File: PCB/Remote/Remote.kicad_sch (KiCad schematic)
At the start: 51 parts, among them J1 LCD, J2 DC, J3 TEMP, J4 LCD, J5 Reset, J6 USB-C-Socket-H, J7 TC2030-USB-NL-DS, T1 T3902_MEMS_Mic, U1 ESP32-S3-MINI-1, U2 SCD41, U3 MD8942, U4 TMP1075DSG, U5 GZP6816D, U7 SHT40, U8 VEML6040

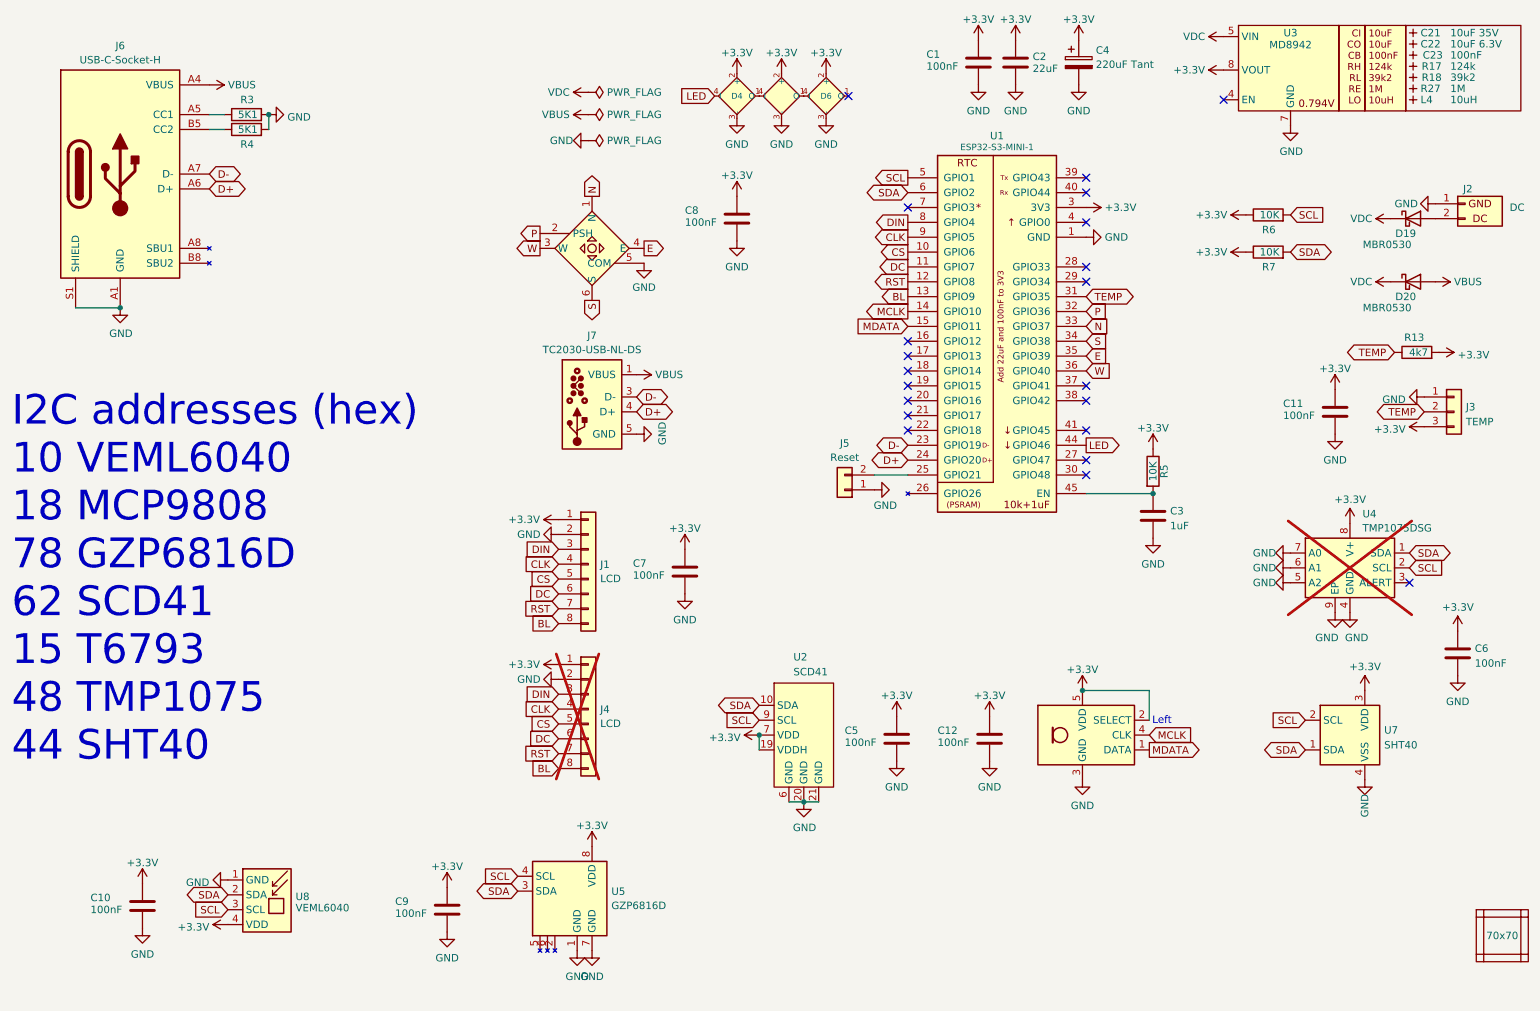
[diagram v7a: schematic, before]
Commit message: Reworked for connecting switch/SCD41
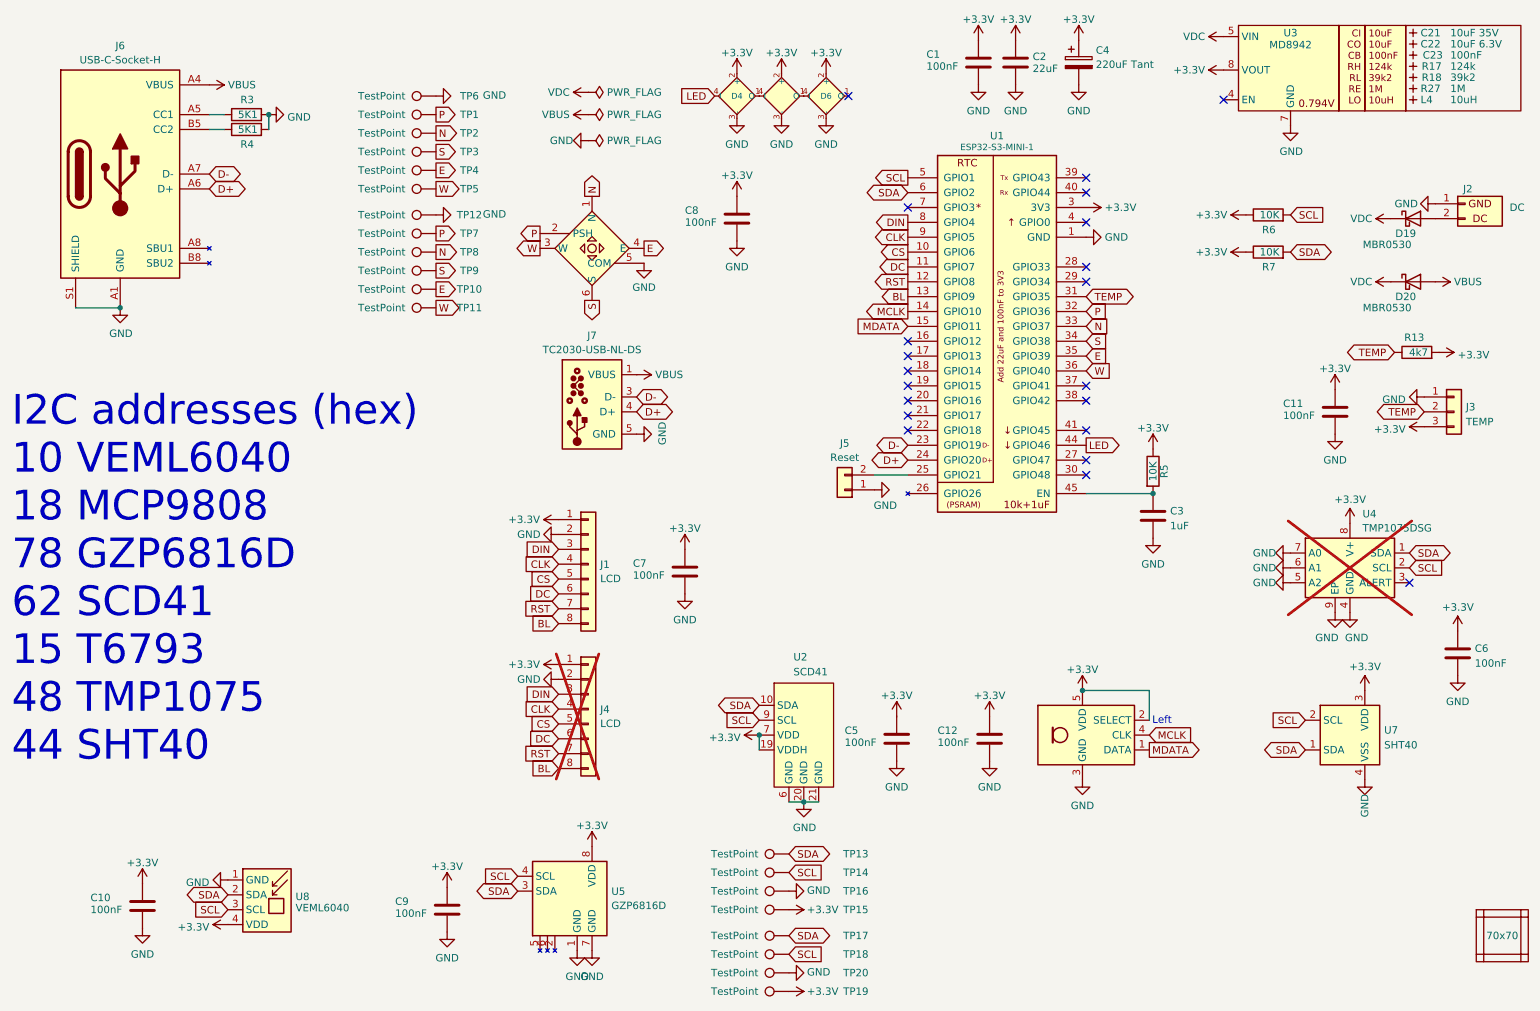
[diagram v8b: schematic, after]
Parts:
- added TP1, TP10, TP11, TP13, TP14, TP15, TP17, TP18, TP19, TP2, TP3, TP4, TP5, TP7, TP8, TP9: TestPoint, RevK:TestPad, symbol Connector:TestPoint
- added TP12, TP16, TP20, TP6: TestPoint, RevK:TestPadSquare, symbol Connector:TestPoint
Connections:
- net +3.3V: now also TP15.1, TP19.1
- net E: now also TP10.1, TP4.1
- net GND: now also TP12.1, TP16.1, TP20.1, TP6.1
- net N: now also TP2.1, TP8.1
- net P: now also TP1.1, TP7.1
- net S: now also TP3.1, TP9.1
- net SCL: now also TP14.1, TP18.1
- net SDA: now also TP13.1, TP17.1
- net W: now also TP11.1, TP5.1
